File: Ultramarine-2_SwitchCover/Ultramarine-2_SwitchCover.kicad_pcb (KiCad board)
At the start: 2 copper layers, 135 x 122.8 mm, 33 parts, among them J1 OLED

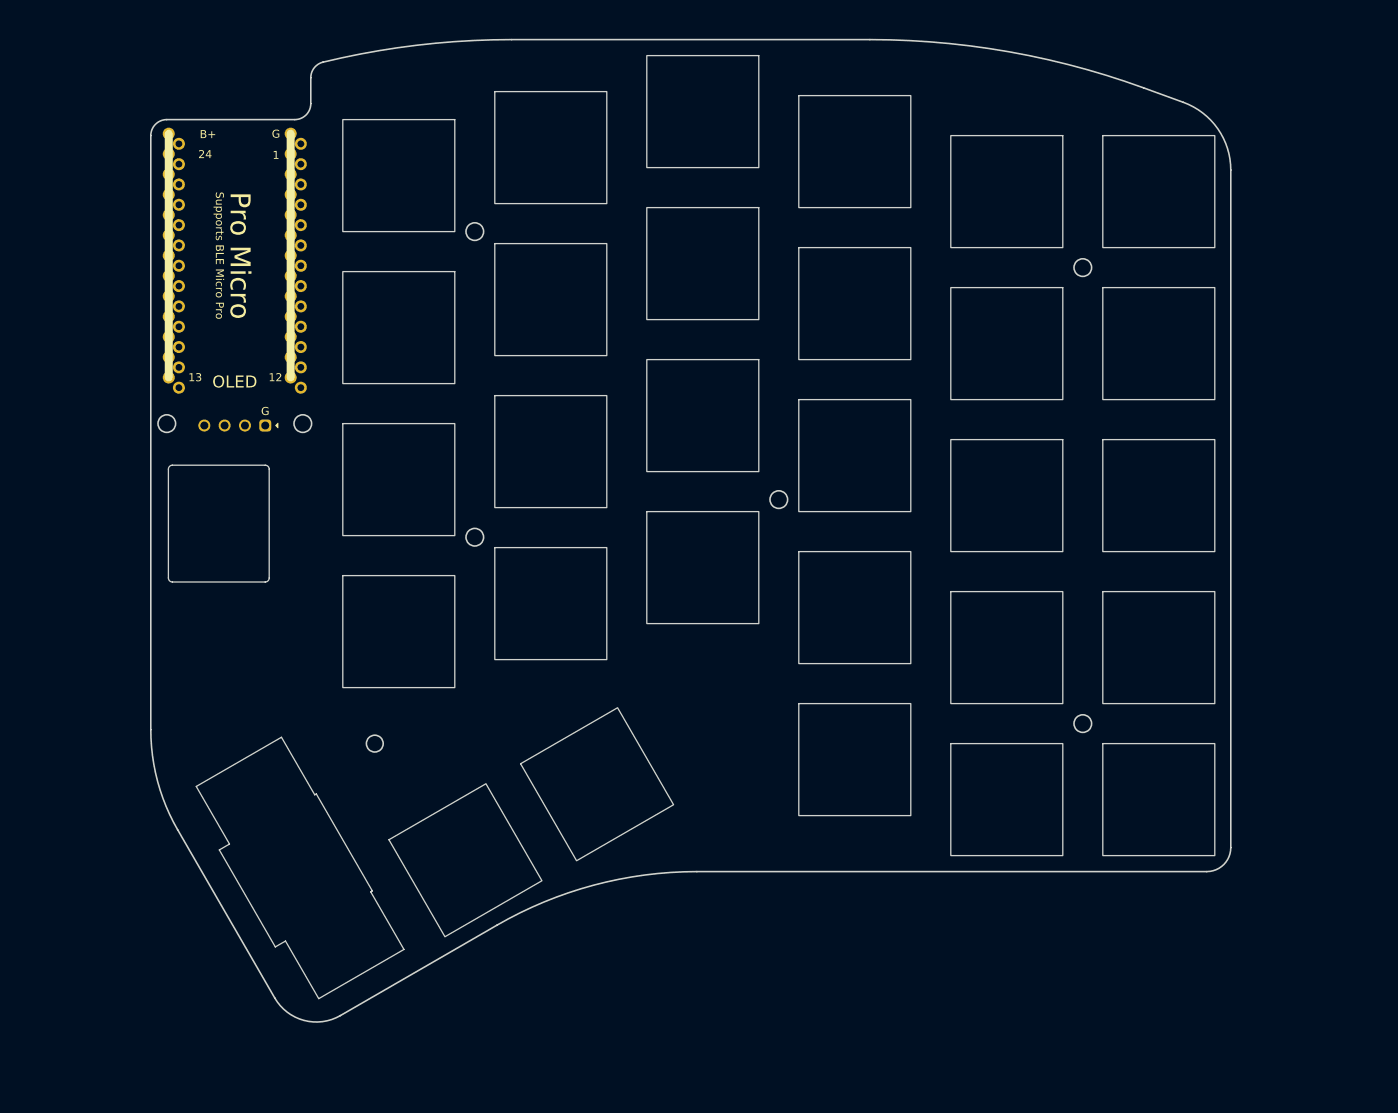
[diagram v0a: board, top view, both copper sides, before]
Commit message: Changed to 6pin connector
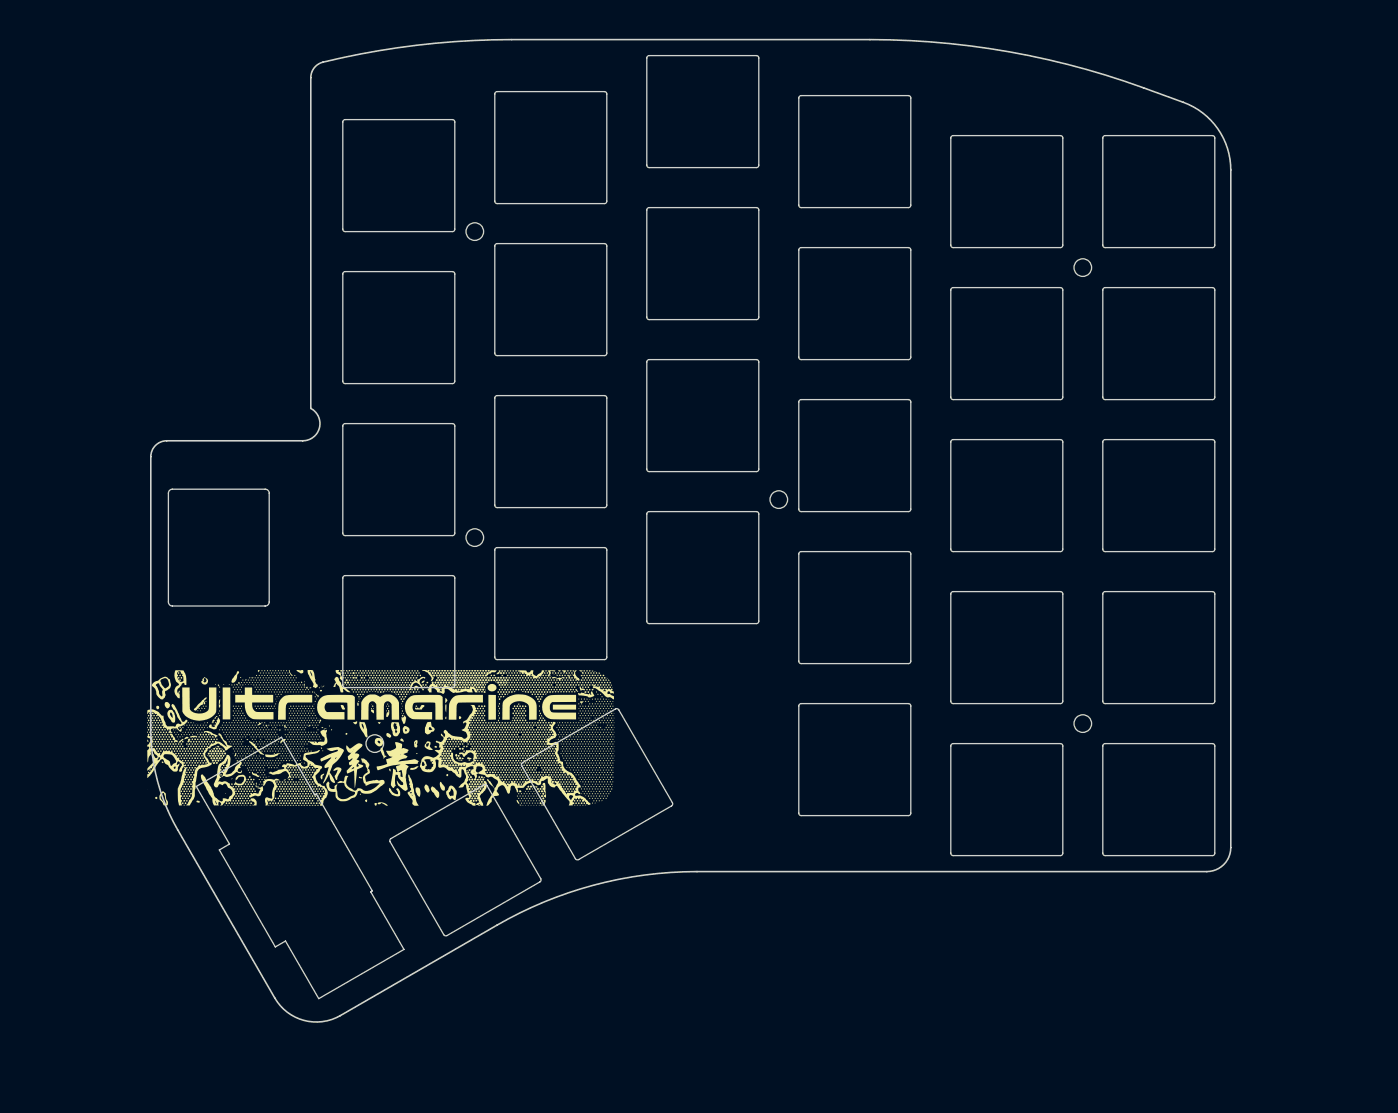
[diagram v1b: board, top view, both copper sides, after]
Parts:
- removed J1: OLED, Ultramarine-2:OLED
- removed U1, U2: ~, Ultramarine-2:BLE Micro Pro
- added G***: LOGO, Ultramarine-2:Ultramarine-2_logo, F.Cu at (114.8, 125.3)
- added REF**: MountingHole_2.2mm_M2, MountingHole:MountingHole_2.2mm_M2, F.Cu at (164.5, 95.5)
- added REF**: MountingHole_2.2mm_M2, MountingHole:MountingHole_2.2mm_M2, F.Cu at (202.5, 66.5)
- added REF**: MountingHole_2.2mm_M2, MountingHole:MountingHole_2.2mm_M2, F.Cu at (114.0, 126.0)
- added REF**: MountingHole_2.2mm_M2, MountingHole:MountingHole_2.2mm_M2, F.Cu at (202.5, 123.5)
- added REF**: MountingHole_2.2mm_M2, MountingHole:MountingHole_2.2mm_M2, F.Cu at (126.5, 100.2)
- added REF**: MountingHole_2.2mm_M2, MountingHole:MountingHole_2.2mm_M2, F.Cu at (126.5, 62.0)
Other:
- outline, holes or cut-outs redrawn
- board text removed: "Ultramarine rev2 Made by Chrodream"

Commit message: completed version
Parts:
- removed G***: LOGO, Ultramarine-2:Ultramarine-2_logo
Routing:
- added copper zone on B.Cu, net (none)
- added copper zone on F.Cu, net (none)
